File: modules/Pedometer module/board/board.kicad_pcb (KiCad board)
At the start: 2 copper layers, 50 x 30 mm, 48 parts, among them IC1 DW01A, J1 USB_C_Receptacle_USB2.0, J2 Conn_01x06_Female, J3 Conn_01x06_Female, J4 Conn_01x06_Female, J6 Conn_01x02_Female, Q1 AO3400A, Q2 AO3401A, Q3 FS8205A, SW1 SW_Push, SW2 SW_Push, SW3 SW_SPST, U1 ME6211, U2 ESP32-WROOM-32D, U3 Inertial_Measurement_Unit, U4 TP4056

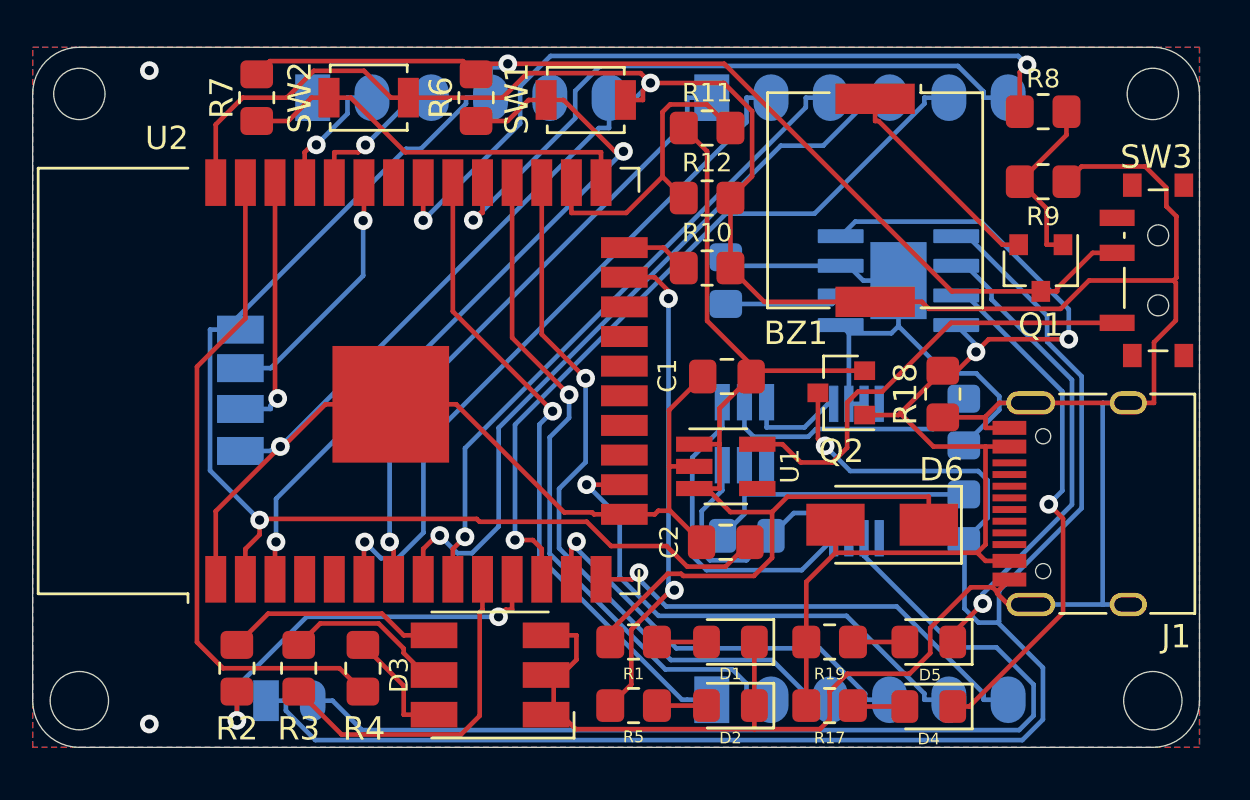
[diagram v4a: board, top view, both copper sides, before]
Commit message: PCB: IMU
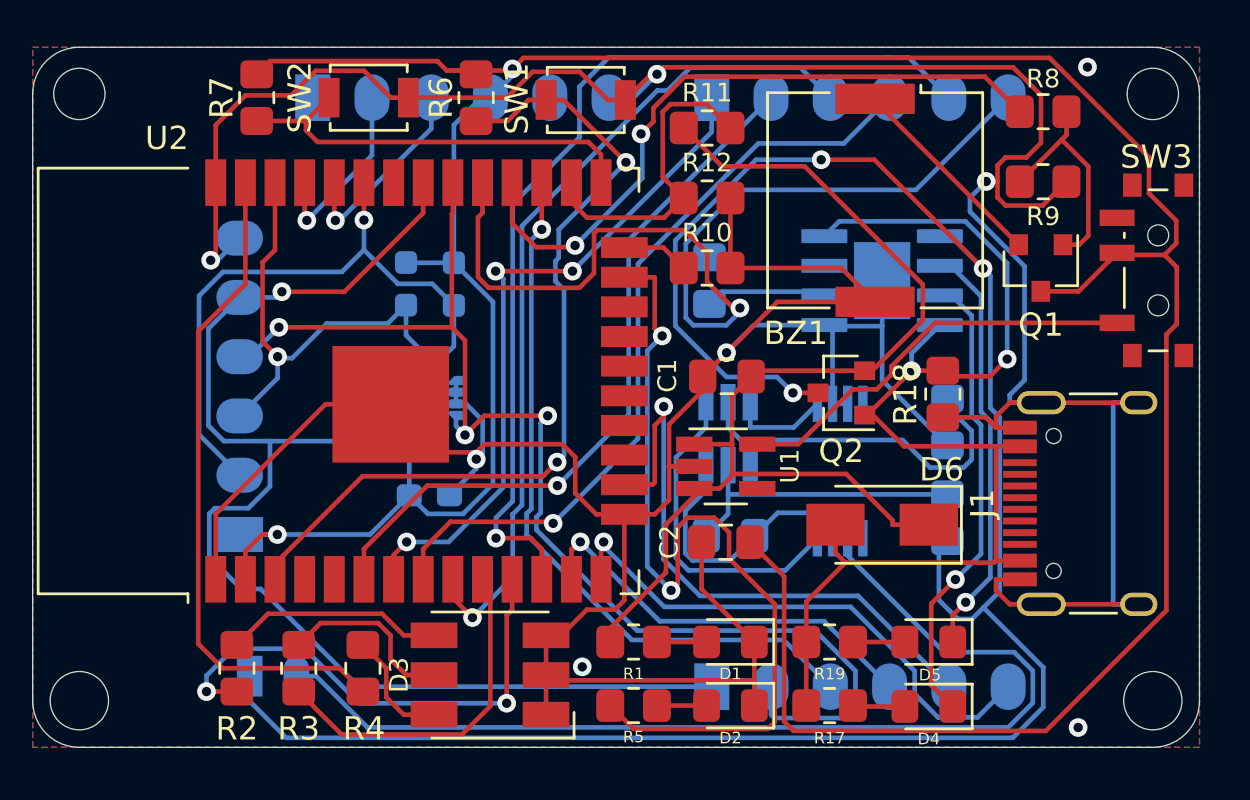
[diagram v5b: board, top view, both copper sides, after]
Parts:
- added C4: 100nF, Capacitor_SMD:C_0603_1608Metric_Pad1.08x0.95mm_HandSolder, B.Cu at (120.0, 104.2)
- added J5: Conn_01x04, Board:SolderWire_1x06_P2.54mm, B.Cu at (111.9, 105.9)
- added R13: 10k, Resistor_SMD:R_0603_1608Metric_Pad0.98x0.95mm_HandSolder, B.Cu at (121.0, 95.2)
- added R14: 10k, Resistor_SMD:R_0603_1608Metric_Pad0.98x0.95mm_HandSolder, B.Cu at (119.0, 95.1)
- J1: footprint Connector_USB:USB_C_Receptacle_HRO_TYPE-C-31-M-12 -> Board:USB_C_Receptacle_HRO_TYPE-C-31-M-12
- U3: value Inertial_Measurement_Unit -> LSM6DS3; footprint Board:Inertial_Measurement_Unit_Board -> Package_LGA:LGA-14_3x2.5mm_P0.5mm_LayoutBorder3x4y
- moved J6 1.26 mm to (112.3, 112.0)
- moved U3 0.72 mm to (120.0, 100.0), turned to 180 degrees
- moved Q3 0.70 mm to (137.6, 103.2)
- moved R20 0.70 mm to (142.2, 105.2)
- moved R22 0.70 mm to (142.2, 101.1)
- moved C3 0.70 mm to (132.9, 105.9)
- moved IC1 0.70 mm to (132.8, 101.6)
- moved R21 0.70 mm to (132.0, 95.0)
- moved U4 0.70 mm to (139.4, 95.0)
- moved J3 0.56 mm to (132.1, 112.4)
- moved J1 0.45 mm to (149.3, 104.5)
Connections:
- J3 pad 1: /IO18 -> INT2
- J3 pad 2: /IO17 -> INT1
- U2 pad 28: /IO17 -> /BUZZER
- U2 pad 30: /IO18 -> INT1
- U2 pad 31: /BUZZER -> INT2
- U2 pad 33: /SDA -> SDA
- U2 pad 36: /SCL -> SCL
- U3 pad 1: +3V3 -> GND
- U3 pad 2: /SDA -> GND
- U3 pad 3: /SCL -> GND
- U3 pad 4: GND -> INT1
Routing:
- net INT2: track 0.00 -> 56.6 mm, vias 0 -> 1
- net INT1: track 0.00 -> 53.3 mm, vias 0 -> 3
- net +3V3: track 95.5 -> 141.2 mm
- net /IO17: track 29.7 -> 0.00 mm, vias 1 -> 0
- net /IO18: track 28.0 -> 0.00 mm, vias 1 -> 0
- net SDA: track 0.00 -> 27.3 mm, vias 0 -> 1
- net SCL: track 0.00 -> 21.1 mm, vias 0 -> 1
- net /IO15: track 21.2 -> 37.5 mm
- net /BMS/BATT+: track 77.7 -> 91.8 mm, vias 1 -> 3
- net /IO5: track 28.9 -> 42.1 mm
- net /SCL: track 11.2 -> 0.00 mm, vias 1 -> 0
- net /SDA: track 10.9 -> 0.00 mm, vias 1 -> 0
- net /IO27: track 32.1 -> 41.5 mm
- net /IO33: track 28.0 -> 36.2 mm
- net GND: track 218.1 -> 212.9 mm, vias 4 -> 8
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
